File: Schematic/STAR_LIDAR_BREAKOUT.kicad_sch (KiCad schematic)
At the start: 4 parts, among them J1 1028585, J2 TBC05-03-1-G-G, Q1 FDD4141

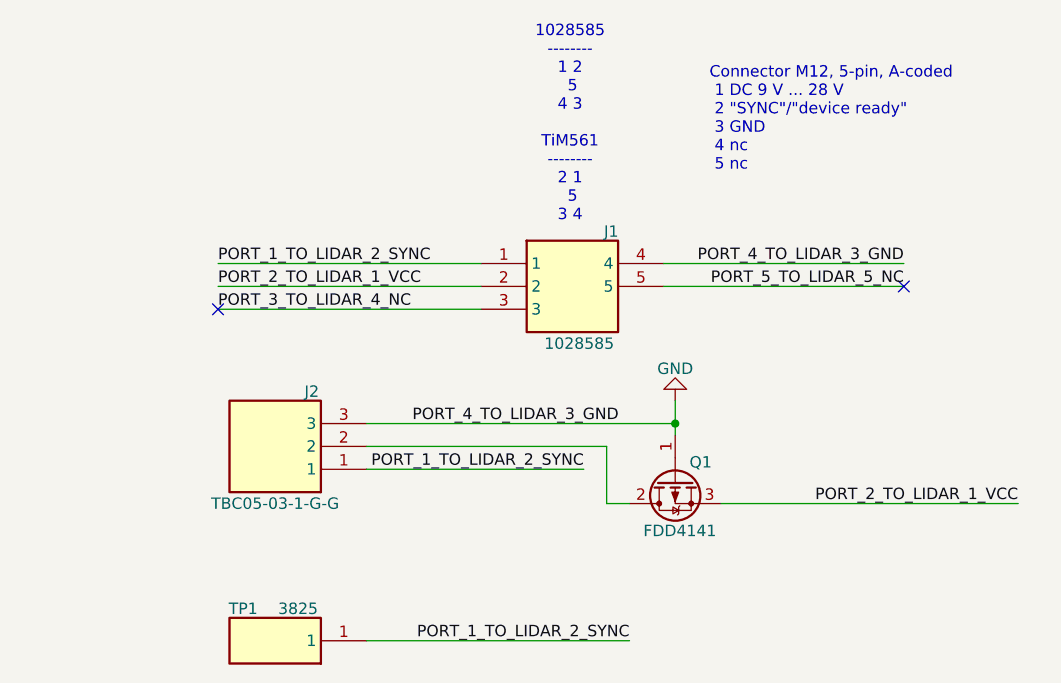
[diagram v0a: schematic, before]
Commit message: put some cheaper parts
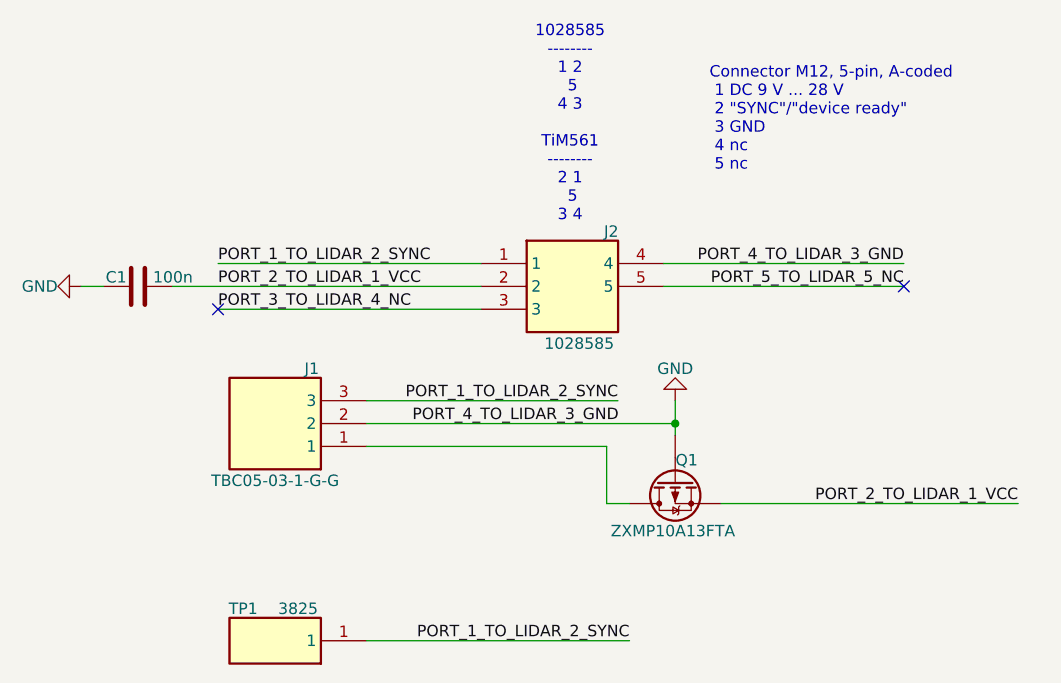
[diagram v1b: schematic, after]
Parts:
- removed Q1: FDD4141, FDD4141:FQD1N80TM, symbol FDD4141:FDD4141
- added C1: 100n, Capacitor_SMD:C_0603_1608Metric_Pad1.08x0.95mm_HandSolder, symbol Device:C
- added Q1: ZXMP10A13FTA, ZXMP10A13FTA:SOT96P240X110-3N, symbol ZXMP10A13FTA:ZXMP10A13FTA
- renumbered J2 to J1, J1 to J2
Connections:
- net GND: now also J1.2, C1.1, Q1.1 (G); no longer J1.3
- net PORT_1_TO_LIDAR_2_SYNC: now also J1.3; no longer J1.1
- net PORT_2_TO_LIDAR_1_VCC: now also C1.2, Q1.3 (S)
- new net: J1.1, Q1.2 (D)
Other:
- moved on the sheet: J1

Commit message: updated lidar breakout board
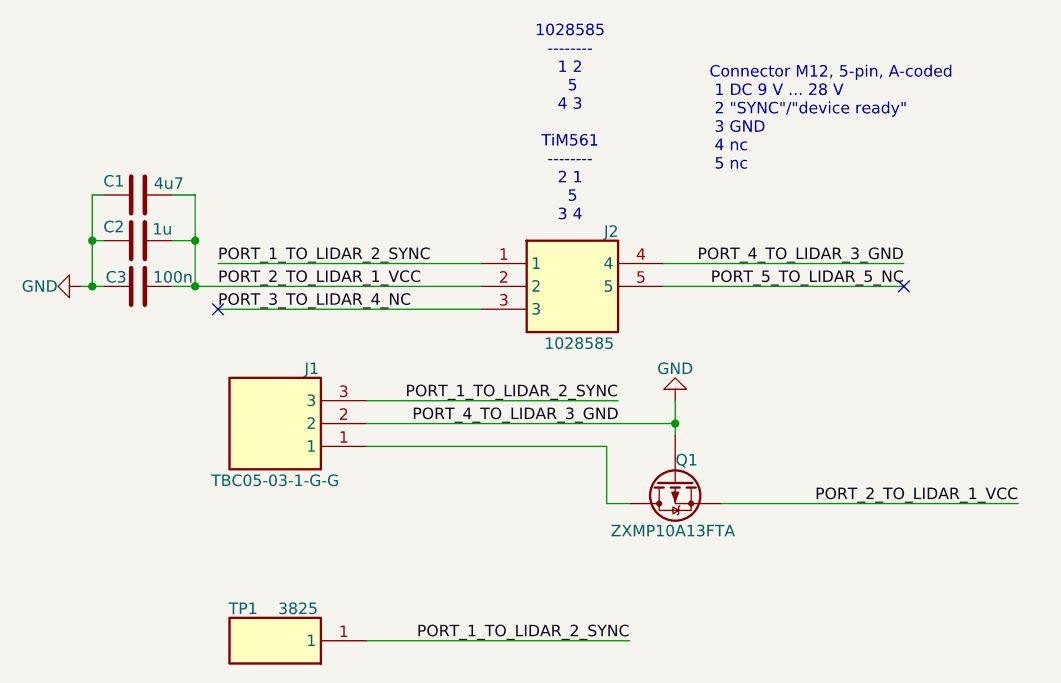
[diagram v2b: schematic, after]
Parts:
- added C1: 4u7, Capacitor_SMD:C_0805_2012Metric_Pad1.18x1.45mm_HandSolder, symbol Device:C
- added C2: 1u, Capacitor_SMD:C_0603_1608Metric_Pad1.08x0.95mm_HandSolder, symbol Device:C
- J1, TP1: now left out of the parts list
- J2: DigiKey Link (none) -> https://www.digikey.com/short/qb0m95mc; DigiKey Part Number (none) -> 277-1028585-ND; DigiKey Price per Unit (none) -> 10.08; Mouser Link (none) -> https://mou.sr/3JIm9TA; Mouser Part Number (none) -> 651-1028585; Mouser Price per Unit (none) -> 13.90
- renumbered C1 to C3
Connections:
- net GND: now also C1.1, C2.1
- net PORT_2_TO_LIDAR_1_VCC: now also C1.2, C2.2
